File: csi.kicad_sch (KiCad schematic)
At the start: 40 parts, among them J15 Bus_DDR4_SODIMM_CUSTOM_Jetson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, T8 BSS138PW, U10 TPS7A0528PDBVR, U11 TLV75512PDBVR, U4 PCA9547_VQFN

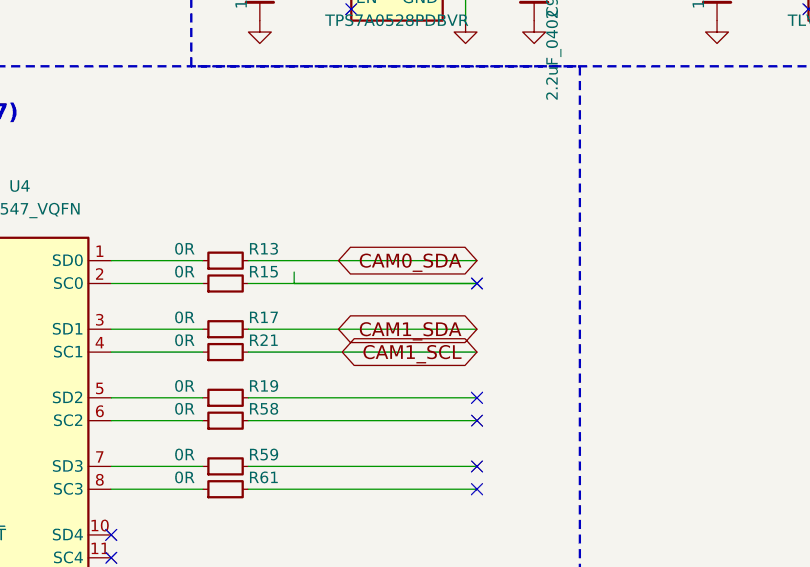
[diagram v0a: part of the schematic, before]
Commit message: fix(csi): restore CAM0_SCL global label at U4 output
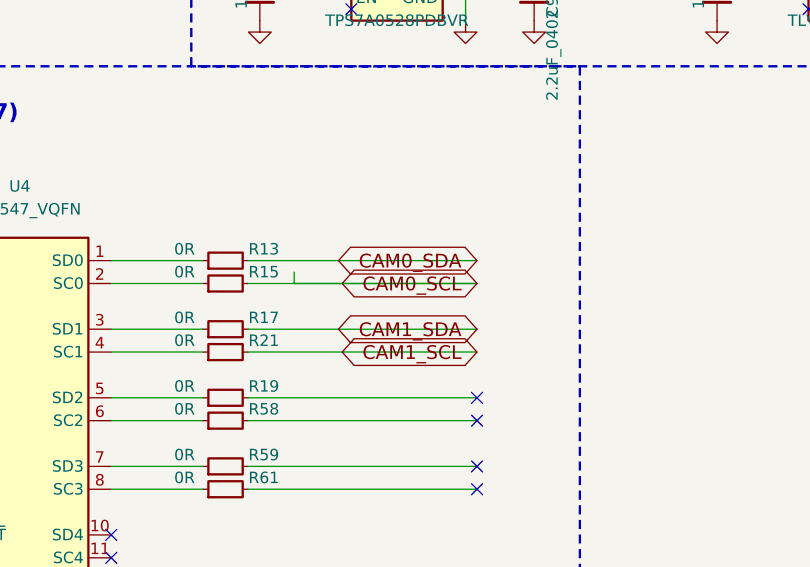
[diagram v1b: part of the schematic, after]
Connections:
- net CAM0_SCL: now also R15.2
- no-connect marks 60 -> 59
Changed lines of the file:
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@@
 	(no_connect (at 70.485 67.31))
 	(no_connect (at 70.485 97.79))
-	(no_connect (at 270.51 212.09))
+	(global_label "CAM0_SCL"
+		(shape bidirectional)
+		(at 270.51 212.09 180)
+		(effects
+			(font
+				(size 1.524 1.524)
+			)
+			(justify right bottom)
+		)
+	)
 	(no_connect (at 270.51 234.95))
 	(no_connect (at 70.485 95.25))

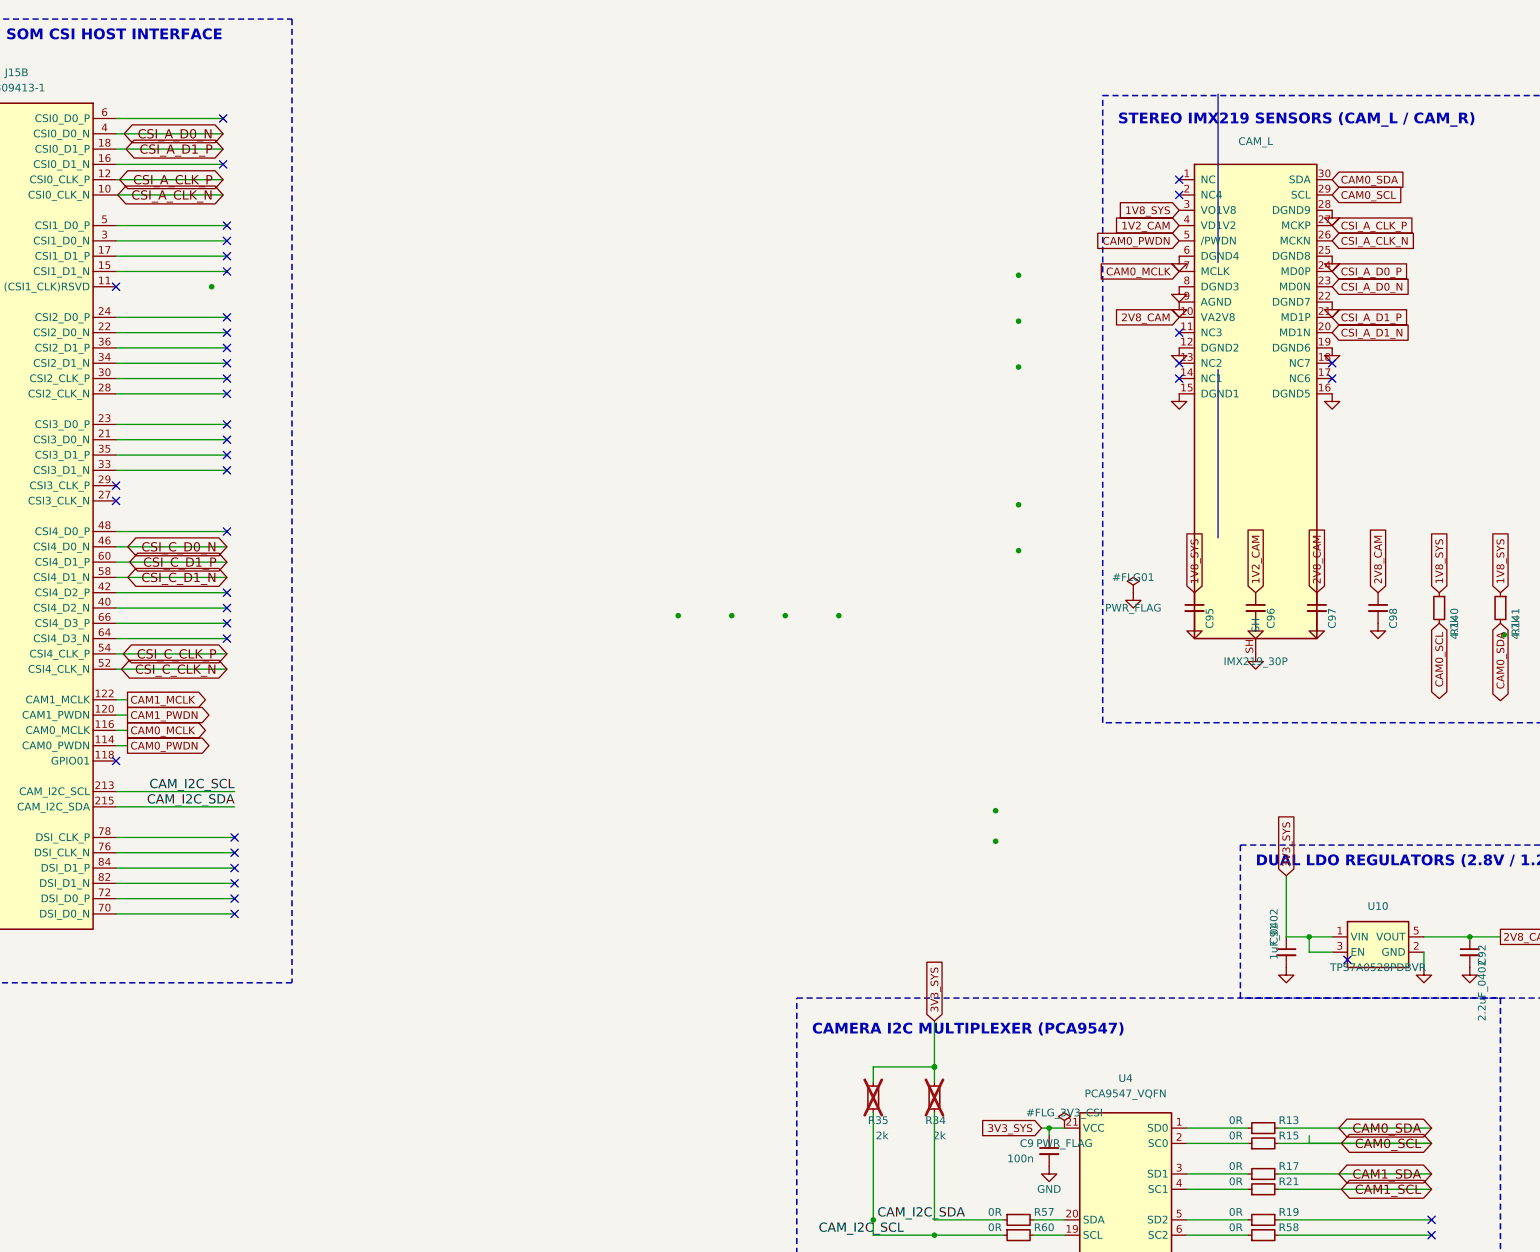
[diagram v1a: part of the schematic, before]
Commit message: fix(schematic): resolve electrical omissions, CSI pairs, CAN power, DNP flags, and ERC stubs
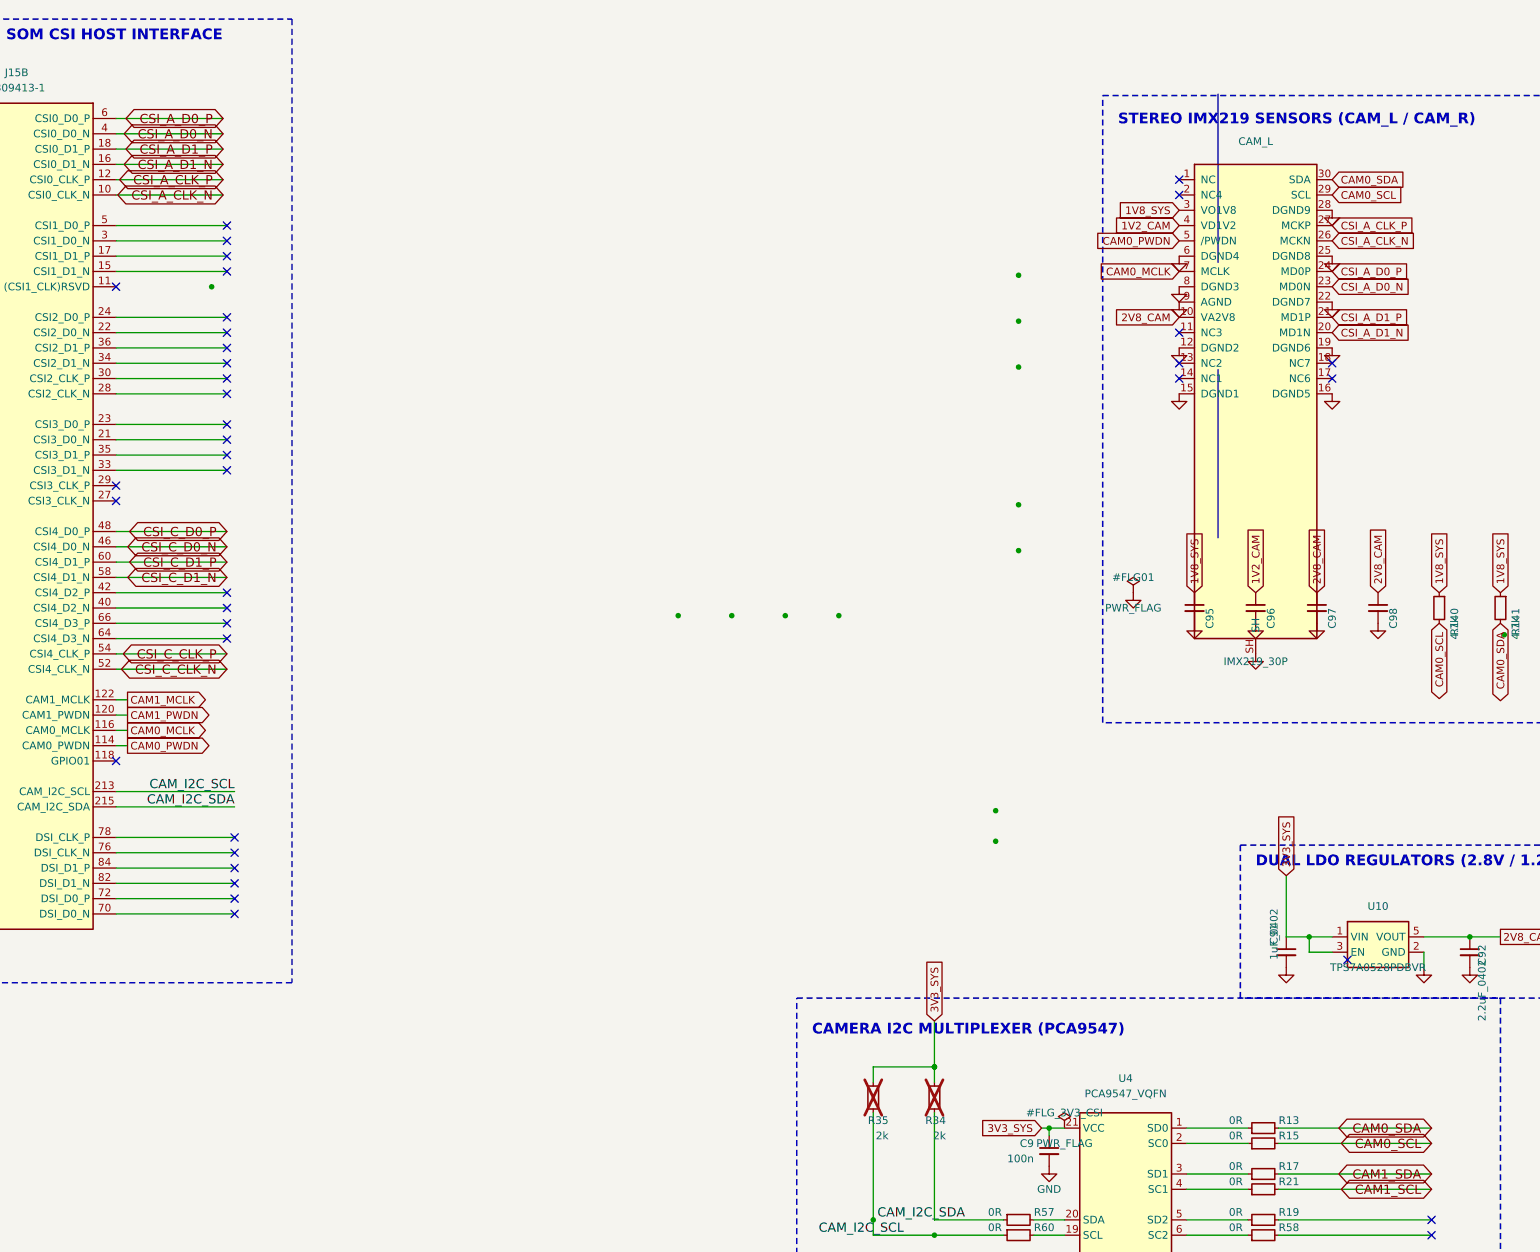
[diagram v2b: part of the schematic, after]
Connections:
- net CSI_A_D0_P: now also J15.6 (CSI0_D0_P)
- net CSI_A_D1_N: now also J15.16 (CSI0_D1_N)
- net CSI_C_D0_P: now also J15.48 (CSI4_D0_P)
- no-connect marks 59 -> 56
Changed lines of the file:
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@@
 	)
 	(no_connect (at 71.755 161.29))
-	(no_connect (at 69.85 49.53))
+	(global_label "CSI_A_D1_N"
+		(shape bidirectional)
+		(at 69.85 49.53 180)
+		(effects
+			(font
+				(size 1.524 1.524)
+			)
+			(justify right bottom)
+		)
+	)
 	(no_connect (at 70.485 85.09))
 	(no_connect (at 70.485 92.71))
@@
 	(no_connect (at 70.485 64.77))
 	(no_connect (at 70.485 120.65))
-	(no_connect (at 69.85 41.91))
+	(global_label "CSI_A_D0_P"
+		(shape bidirectional)
+		(at 69.85 41.91 180)
+		(effects
+			(font
+				(size 1.524 1.524)
+			)
+			(justify right bottom)
+		)
+	)
 	(no_connect (at 270.51 232.41))
 	(global_label "CSI_A_D1_P"
@@
 	(no_connect (at 270.51 234.95))
 	(no_connect (at 70.485 95.25))
-	(no_connect (at 70.485 110.49))
+	(global_label "CSI_C_D0_P"
+		(shape bidirectional)
+		(at 70.485 110.49 180)
+		(effects
+			(font
+				(size 1.524 1.524)
+			)
+			(justify right bottom)
+		)
+	)
 	(no_connect (at 70.485 100.33))
 	(no_connect (at 70.485 125.73))
@@
 	)
 	(wire
-		(pts
-			(xy 250.19 210.82) (xy 250.19 212.09)
-		)
-		(stroke (width 0) (type default))
-	)
-	(wire
-		(pts
-			(xy 250.19 212.09) (xy 270.51 212.09)
-		)
-		(stroke (width 0) (type default))
-	)
-	(wire

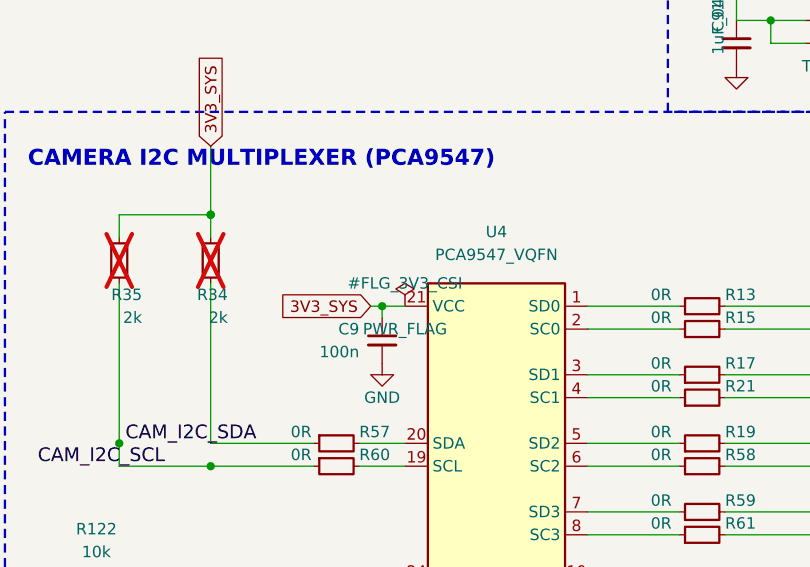
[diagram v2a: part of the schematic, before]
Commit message: feat(release): resolve all ERC/DRC/parity issues, complete 8-layer routing, and generate JLCPCB fab outputs
Resolve all schematic ERC violations, PCB DRC errors/warnings, schematic-to-PCB parity mismatches, and LCSC BOM/CPL fields, and package 8-layer Gerbers, drills, BOM, and CPL for JLCPCB manufacturing.

Co-Authored-By: CopperPilot <noreply@copperpilot.ai>
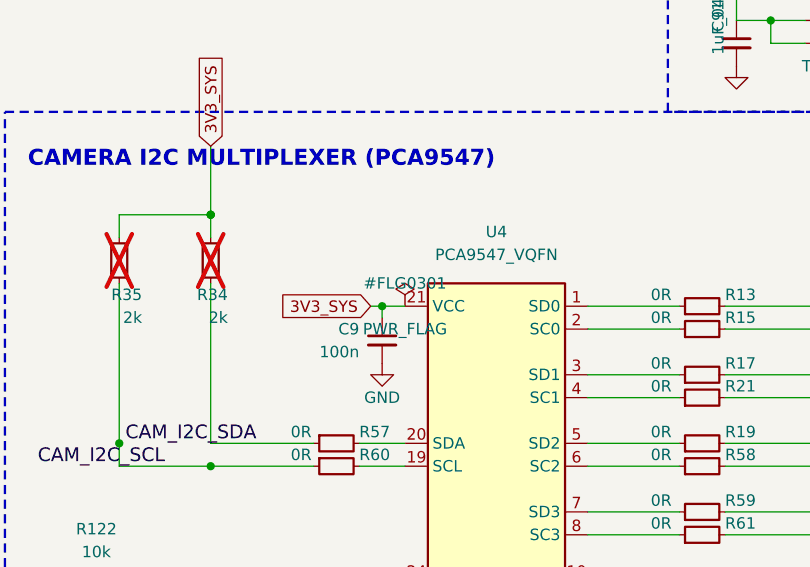
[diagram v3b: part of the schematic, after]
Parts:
- C100, C101, C95, C96, C97, C99: LCSC (none) -> C1525; MPN (none) -> GRM155R61H104KE14D
- C102, C92, C94, C98: LCSC (none) -> C12530; MPN (none) -> C1005X5R1A225K050BC
- C9: LCSC (none) -> C1525
- C91, C93: LCSC (none) -> C52923; MPN (none) -> C1005X6S1A105K050BC
- CAM_L, CAM_R: LCSC (none) -> C424662; MPN (none) -> BM20B(0.8)-30DS-0.4V(51)
- J15: LCSC (none) -> C429199
- R122: LCSC (none) -> C25744
- R13, R15, R17, R19, R21, R57, R58, R59, R60, R61: LCSC (none) -> C17168
- R140, R141, R142, R143: LCSC (none) -> C25900; MPN (none) -> CR0402-FX-4701GLF
- R144, R145: LCSC (none) -> C25741; MPN (none) -> CR0402-FX-1003GLF
- R34, R35: LCSC (none) -> C4109
- R69: LCSC (none) -> C25741
- T8: LCSC (none) -> C84617
- U10: LCSC (none) -> C194387; MPN (none) -> TPS7A0528PDBVR
- U11: LCSC (none) -> C485675; MPN (none) -> TLV75512PDBVR
- U4: LCSC (none) -> C138804

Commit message: fix(sch): resolve all symbol, label, property, and frame collisions on CSI sheet (Page 3)
Fix IMX219_30P symbol body height and SH pin placement, add wire stubs and outward justifications on all CAM_L/CAM_R/J15B/U4 global labels, rotate side GND symbols outward, unstack C95-C102/R140-R145/C91-C94/R13-R61 properties, shift U11 LDO block for clearance, and delete 24 stray junctions and 5 stray polylines.

Co-Authored-By: CopperPilot <noreply@copperpilot.ai>
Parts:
- C100, C101, C95, C96, C97, C99: value C_100n_0402 -> 100n
- C102, C98: value C_2u2_0402 -> 2u2
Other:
- moved on the sheet: C93, C94, CAM_L, CAM_R, U11
